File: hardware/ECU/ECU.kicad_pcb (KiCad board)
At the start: 2 copper layers, 115 x 100 mm, 112 parts, among them IC1 IR4427SPBF, IC2 EL357NB_TA_-G, IC3 EL357NB_TA_-G, IC4 ESP32-S3-WROOM-1U-N8R8, IC5 EL357NB_TA_-G, J1 AQS, J2 TFP09-2-12B, J3 CAM_SENSOR, J4 USB_B, J5 BATTERY, J6 GATEs, J7 ISC Control, J8 CAPTURE_TRG, Q1 RJP63K2, Q3 RJP63K2, Q4 RJP63K2, SW1 RESET BTN, SW2 ZERO BTN, U1 LM2576S-5, U2 AMS1117-3.3, U3 L293D, U4 ADS1115IDGS, U5 ADS1115IDGS, U6 INA180A3, U7 SRV05-4

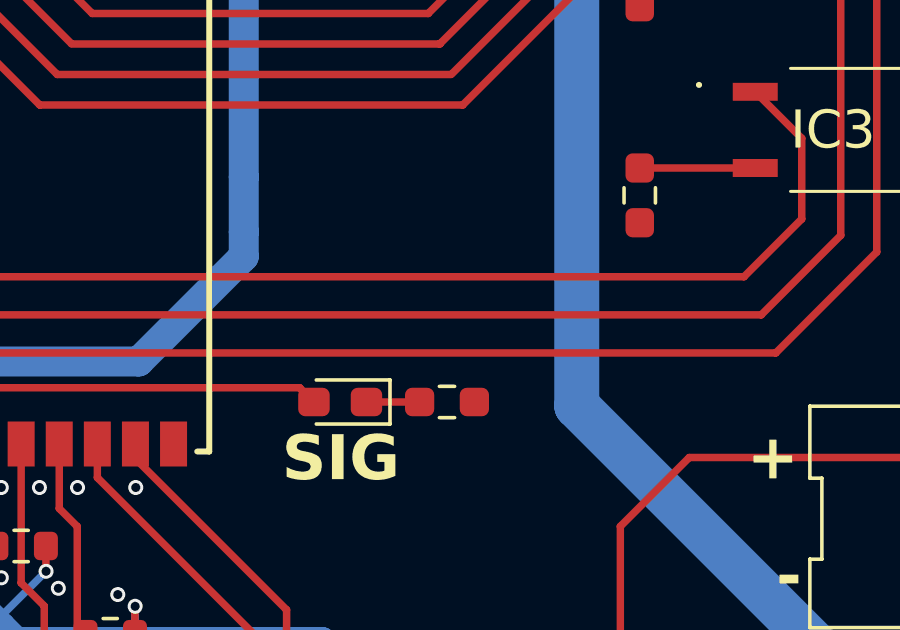
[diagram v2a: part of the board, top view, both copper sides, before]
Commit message: fix gerber file containing deleted layers
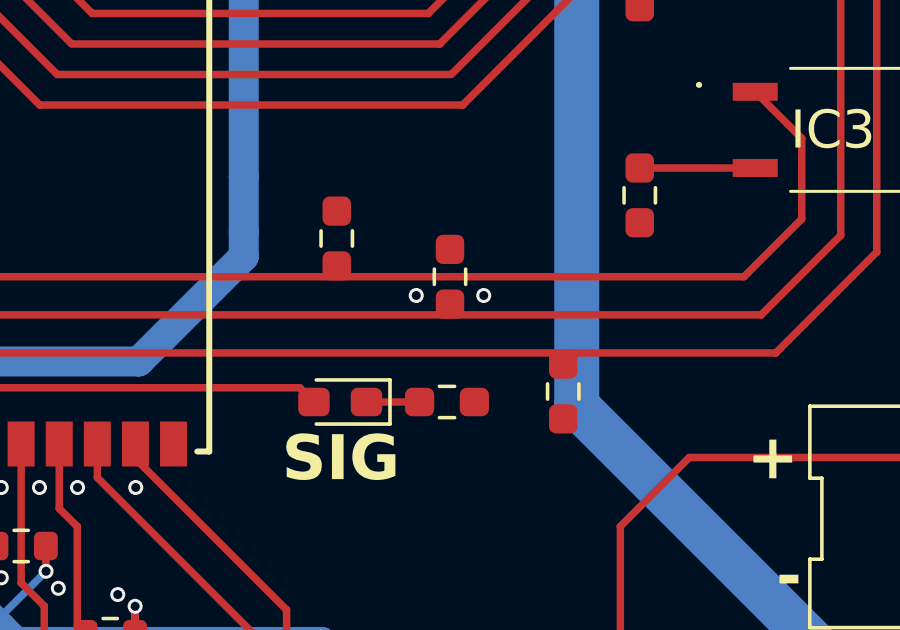
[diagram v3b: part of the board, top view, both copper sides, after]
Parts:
- added R40: 1k, Resistor_SMD:R_0603_1608Metric_Pad0.98x0.95mm_HandSolder, F.Cu at (143.9, 113.0)
- added R41: 1k, Resistor_SMD:R_0603_1608Metric_Pad0.98x0.95mm_HandSolder, F.Cu at (147.7, 114.2)
- added R44: 1k, Resistor_SMD:R_0603_1608Metric_Pad0.98x0.95mm_HandSolder, F.Cu at (151.4, 118.0)
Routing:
- net GND: vias 233 -> 235
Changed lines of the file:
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@@
   )
   (footprint "Resistor_SMD:R_0603_1608Metric_Pad0.98x0.95mm_HandSolder" (layer "F.Cu")
+    (at 147.675 114.225 90)
+    (descr "Resistor SMD 0603 (1608 Metric), square (rectangular) end terminal, IPC_7351 nominal with elongated pad for handsoldering. (Body size source: IPC-SM-782 page 72, https://www.pcb-3d.com/wordpress/wp-content/uploads/ipc-sm-782a_amendment_1_and_2.pdf), generated with kicad-footprint-generator")
+    (tags "resistor handsolder")
+    (property "Sheetfile" "ECU.kicad_sch")
+    (property "Sheetname" "")
+    (property "ki_description" "Resistor")
+    (property "ki_keywords" "R res resistor")
+    (attr smd)
+    (fp_text reference "R41" (at 0 -1.43 90) (layer "F.SilkS") hide
+        (effects (font (size 1 1) (thickness 0.15)))
+    )
+    (fp_text value "1k" (at 0 1.43 90) (layer "F.Fab")
+        (effects (font (size 1 1) (thickness 0.15)))
+    )
+    (fp_text user "${REFERENCE}" (at 0 0 90) (layer "F.Fab")
+        (effects (font (size 0.4 0.4) (thickness 0.06)))
+    )
+    (fp_line (start -0.254724 -0.5225) (end 0.254724 -0.5225)
+      (stroke (width 0.12) (type solid)) (layer "F.SilkS"))
+    (fp_line (start -0.254724 0.5225) (end 0.254724 0.5225)
+      (stroke (width 0.12) (type solid)) (layer "F.SilkS"))
+    (fp_line (start -1.65 -0.73) (end 1.65 -0.73)
+      (stroke (width 0.05) (type solid)) (layer "F.CrtYd"))
+    (fp_line (start -1.65 0.73) (end -1.65 -0.73)
+      (stroke (width 0.05) (type solid)) (layer "F.CrtYd"))
+    (fp_line (start 1.65 -0.73) (end 1.65 0.73)
+      (stroke (width 0.05) (type solid)) (layer "F.CrtYd"))
+    (fp_line (start 1.65 0.73) (end -1.65 0.73)
+      (stroke (width 0.05) (type solid)) (layer "F.CrtYd"))
+    (fp_line (start -0.8 -0.4125) (end 0.8 -0.4125)
+      (stroke (width 0.1) (type solid)) (layer "F.Fab"))
+    (fp_line (start -0.8 0.4125) (end -0.8 -0.4125)
+      (stroke (width 0.1) (type solid)) (layer "F.Fab"))
+    (fp_line (start 0.8 -0.4125) (end 0.8 0.4125)
+      (stroke (width 0.1) (type solid)) (layer "F.Fab"))
+    (fp_line (start 0.8 0.4125) (end -0.8 0.4125)
+      (stroke (width 0.1) (type solid)) (layer "F.Fab"))
+    (pad "1" smd roundrect (at -0.9125 0 90) (size 0.975 0.95) (layers "F.Cu" "F.Paste" "F.Mask") (roundrect_rratio 0.25)
+      (net 12 "/FUEL_PIN") (pintype "passive"))
+    (pad "2" smd roundrect (at 0.9125 0 90) (size 0.975 0.95) (layers "F.Cu" "F.Paste" "F.Mask") (roundrect_rratio 0.25)
+      (net 1 "GND") (pintype "passive"))
+    (model "${KICAD6_3DMODEL_DIR}/Resistor_SMD.3dshapes/R_0603_1608Metric.wrl"
+      (offset (xyz 0 0 0))
+      (scale (xyz 1 1 1))
+      (rotate (xyz 0 0 0))
+    )
+  )
+  (footprint "Resistor_SMD:R_0603_1608Metric_Pad0.98x0.95mm_HandSolder" (layer "F.Cu")
     (at 154 97.1125 90)
     (descr "Resistor SMD 0603 (1608 Metric), square (rectangular) end terminal, IPC_7351 nominal with elongated pad for handsoldering. (Body size source: IPC-SM-782 page 72, https://www.pcb-3d.com/wordpress/wp-content/uploads/ipc-sm-782a_amendment_1_and_2.pdf), generated with kicad-footprint-generator")
@@
     )
   )
+  (footprint "Resistor_SMD:R_0603_1608Metric_Pad0.98x0.95mm_HandSolder" (layer "F.Cu")
+    (at 143.9 112.95 90)
+    (descr "Resistor SMD 0603 (1608 Metric), square (rectangular) end terminal, IPC_7351 nominal with elongated pad for handsoldering. (Body size source: IPC-SM-782 page 72, https://www.pcb-3d.com/wordpress/wp-content/uploads/ipc-sm-782a_amendment_1_and_2.pdf), generated with kicad-footprint-generator")
+    (tags "resistor handsolder")
+    (property "Sheetfile" "ECU.kicad_sch")
+    (property "Sheetname" "")
+    (property "ki_description" "Resistor")
+    (property "ki_keywords" "R res resistor")
+    (attr smd)
+    (fp_text reference "R40" (at 0 -1.43 90) (layer "F.SilkS") hide
+        (effects (font (size 1 1) (thickness 0.15)))
+    )
+    (fp_text value "1k" (at 0 1.43 90) (layer "F.Fab")
+        (effects (font (size 1 1) (thickness 0.15)))
+    )
+    (fp_text user "${REFERENCE}" (at 0 0 90) (layer "F.Fab")
+        (effects (font (size 0.4 0.4) (thickness 0.06)))
+    )
+    (fp_line (start -0.254724 -0.5225) (end 0.254724 -0.5225)
+      (stroke (width 0.12) (type solid)) (layer "F.SilkS"))
+    (fp_line (start -0.254724 0.5225) (end 0.254724 0.5225)
+      (stroke (width 0.12) (type solid)) (layer "F.SilkS"))
+    (fp_line (start -1.65 -0.73) (end 1.65 -0.73)
+      (stroke (width 0.05) (type solid)) (layer "F.CrtYd"))
+    (fp_line (start -1.65 0.73) (end -1.65 -0.73)
+      (stroke (width 0.05) (type solid)) (layer "F.CrtYd"))
+    (fp_line (start 1.65 -0.73) (end 1.65 0.73)
+      (stroke (width 0.05) (type solid)) (layer "F.CrtYd"))
+    (fp_line (start 1.65 0.73) (end -1.65 0.73)
+      (stroke (width 0.05) (type solid)) (layer "F.CrtYd"))
+    (fp_line (start -0.8 -0.4125) (end 0.8 -0.4125)
+      (stroke (width 0.1) (type solid)) (layer "F.Fab"))
+    (fp_line (start -0.8 0.4125) (end -0.8 -0.4125)
+      (stroke (width 0.1) (type solid)) (layer "F.Fab"))
+    (fp_line (start 0.8 -0.4125) (end 0.8 0.4125)
+      (stroke (width 0.1) (type solid)) (layer "F.Fab"))
+    (fp_line (start 0.8 0.4125) (end -0.8 0.4125)
+      (stroke (width 0.1) (type solid)) (layer "F.Fab"))
+    (pad "1" smd roundrect (at -0.9125 0 90) (size 0.975 0.95) (layers "F.Cu" "F.Paste" "F.Mask") (roundrect_rratio 0.25)
+      (net 11 "/COIL_PIN") (pintype "passive"))
+    (pad "2" smd roundrect (at 0.9125 0 90) (size 0.975 0.95) (layers "F.Cu" "F.Paste" "F.Mask") (roundrect_rratio 0.25)
+      (net 1 "GND") (pintype "passive"))
+    (model "${KICAD6_3DMODEL_DIR}/Resistor_SMD.3dshapes/R_0603_1608Metric.wrl"
+      (offset (xyz 0 0 0))
+      (scale (xyz 1 1 1))
+      (rotate (xyz 0 0 0))
+    )
+  )
   (footprint "Button_Switch_SMD:SW_SPST_PTS810" (layer "F.Cu")
     (at 136.77 81.375 90)
@@
     )
   )
+  (footprint "Resistor_SMD:R_0603_1608Metric_Pad0.98x0.95mm_HandSolder" (layer "F.Cu")
+    (at 151.45 118.05 -90)
+    (descr "Resistor SMD 0603 (1608 Metric), square (rectangular) end terminal, IPC_7351 nominal with elongated pad for handsoldering. (Body size source: IPC-SM-782 page 72, https://www.pcb-3d.com/wordpress/wp-content/uploads/ipc-sm-782a_amendment_1_and_2.pdf), generated with kicad-footprint-generator")
+    (tags "resistor handsolder")
+    (property "Sheetfile" "ECU.kicad_sch")
+    (property "Sheetname" "")
+    (property "ki_description" "Resistor")
+    (property "ki_keywords" "R res resistor")
+    (attr smd)
+    (fp_text reference "R44" (at 0 -1.43 90) (layer "F.SilkS") hide
+        (effects (font (size 1 1) (thickness 0.15)))
+    )
+    (fp_text value "1k" (at 0 1.43 90) (layer "F.Fab")
+        (effects (font (size 1 1) (thickness 0.15)))
+    )
+    (fp_text user "${REFERENCE}" (at 0 0 90) (layer "F.Fab")
+        (effects (font (size 0.4 0.4) (thickness 0.06)))
+    )
+    (fp_line (start -0.254724 -0.5225) (end 0.254724 -0.5225)
+      (stroke (width 0.12) (type solid)) (layer "F.SilkS"))
+    (fp_line (start -0.254724 0.5225) (end 0.254724 0.5225)
+      (stroke (width 0.12) (type solid)) (layer "F.SilkS"))
+    (fp_line (start -1.65 -0.73) (end 1.65 -0.73)
+      (stroke (width 0.05) (type solid)) (layer "F.CrtYd"))
+    (fp_line (start -1.65 0.73) (end -1.65 -0.73)
+      (stroke (width 0.05) (type solid)) (layer "F.CrtYd"))
+    (fp_line (start 1.65 -0.73) (end 1.65 0.73)
+      (stroke (width 0.05) (type solid)) (layer "F.CrtYd"))
+    (fp_line (start 1.65 0.73) (end -1.65 0.73)
+      (stroke (width 0.05) (type solid)) (layer "F.CrtYd"))
+    (fp_line (start -0.8 -0.4125) (end 0.8 -0.4125)
+      (stroke (width 0.1) (type solid)) (layer "F.Fab"))
+    (fp_line (start -0.8 0.4125) (end -0.8 -0.4125)
+      (stroke (width 0.1) (type solid)) (layer "F.Fab"))
+    (fp_line (start 0.8 -0.4125) (end 0.8 0.4125)
+      (stroke (width 0.1) (type solid)) (layer "F.Fab"))
+    (fp_line (start 0.8 0.4125) (end -0.8 0.4125)
+      (stroke (width 0.1) (type solid)) (layer "F.Fab"))
+    (pad "1" smd roundrect (at -0.9125 0 270) (size 0.975 0.95) (layers "F.Cu" "F.Paste" "F.Mask") (roundrect_rratio 0.25)
+      (net 33 "/FUEL_PUMP_PIN") (pintype "passive"))
+    (pad "2" smd roundrect (at 0.9125 0 270) (size 0.975 0.95) (layers "F.Cu" "F.Paste" "F.Mask") (roundrect_rratio 0.25)
+      (net 1 "GND") (pintype "passive"))
+    (model "${KICAD6_3DMODEL_DIR}/Resistor_SMD.3dshapes/R_0603_1608Metric.wrl"
+      (offset (xyz 0 0 0))
+      (scale (xyz 1 1 1))
+      (rotate (xyz 0 0 0))
+    )
+  )
   (footprint "Capacitor_SMD:C_0805_2012Metric_Pad1.18x1.45mm_HandSolder" (layer "F.Cu")
     (at 119.0375 125.2)
@@
   (via (at 185.91 94.4) (size 0.5) (drill 0.3) (layers "F.Cu" "B.Cu") (free) (net 1))
   (via (at 157.8 140.6) (size 0.5) (drill 0.3) (layers "F.Cu" "B.Cu") (free) (net 1))
+  (via (at 146.55 114.85) (size 0.5) (drill 0.3) (layers "F.Cu" "B.Cu") (free) (net 1))
   (via (at 152.1 81.497741) (size 0.5) (drill 0.3) (layers "F.Cu" "B.Cu") (free) (net 1))
   (via (at 159.49 133.62) (size 0.5) (drill 0.3) (layers "F.Cu" "B.Cu") (net 1))
@@
   (via (at 144.6 81.497741) (size 0.5) (drill 0.3) (layers "F.Cu" "B.Cu") (free) (net 1))
   (via (at 162 140.6) (size 0.5) (drill 0.3) (layers "F.Cu" "B.Cu") (free) (net 1))
+  (via (at 148.8 114.85) (size 0.5) (drill 0.3) (layers "F.Cu" "B.Cu") (free) (net 1))
   (via (at 202.7 124.2) (size 0.5) (drill 0.3) (layers "F.Cu" "B.Cu") (free) (net 1))
   (via (at 163 78.4) (size 0.5) (drill 0.3) (layers "F.Cu" "B.Cu") (free) (net 1))
